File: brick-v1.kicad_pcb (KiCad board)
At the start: 2 copper layers, 28 x 41 mm, 15 parts, among them J1 buzzer_toggle_pin, J2 battery_header, U1 Teensy4.1, U2 voltReg

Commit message: v1.3 update
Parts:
- removed J2: battery_header, Connector_PinSocket_2.54mm:PinSocket_1x02_P2.54mm_Horizontal
- removed Logo0: ~, rrc_logo:RRC_logo
- removed R4: R-Device, Resistor_THT:R_Axial_DIN0207_L6.3mm_D2.5mm_P10.16mm_Horizontal
- removed S2: BN220-GPS, rrc_bn220_gps:BN220
- added Logo1: ~, rrc_logo:tmu, F.Cu at (175.8, 49.8)
- added TH1: Thermistor, Resistor_THT:R_Axial_DIN0922_L20.0mm_D9.0mm_P25.40mm_Horizontal, F.Cu at (179.1, 36.8)
- added U3: Teensy4.1, rrc_teensy:Teensy41, F.Cu at (201.9, 81.3)
- I1: value INA260 -> MPU6050; footprint rrc_INA260:INA260 -> rrc_MPU6050:MPU6050
- I2: value MPU6050 -> INA260; footprint rrc_MPU6050:MPU6050 -> rrc_INA260:INA260
- J1: value buzzer_toggle_pin -> battery_header; footprint Connector_PinHeader_2.54mm:PinHeader_1x03_P2.54mm_Vertical -> Connector_PinSocket_2.54mm:PinSocket_1x02_P2.54mm_Horizontal
- S1: value RFD900+-RF_Module -> BN220-GPS; footprint rrc_rfd900+:RFD900+ -> rrc_bn220_gps:BN220
- U1: value Teensy4.1 -> XB3-24Z8CM-J; footprint rrc_teensy:Teensy41 -> RRC_footprint:xbee_s2c
- U2: value voltReg -> L7805; footprint rrc_voltReg:voltReg2 -> Connector_PinHeader_2.54mm:PinHeader_1x03_P2.54mm_Vertical
- moved U2 107.0 mm to (221.0, 50.8)
- moved S1 71.0 mm to (175.9, 89.6)
- moved I2 70.4 mm to (201.9, 57.1)
- moved I3 56.3 mm to (166.4, 108.2)
- moved I1 53.3 mm to (158.8, 69.8)
- moved BZ1 44.6 mm to (161.3, 34.3)
- moved U1 30.9 mm to (207.9, 96.1), turned to -90 degrees
- moved J1 20.8 mm to (219.0, 34.3)
- moved R1 6.38 mm to (174.0, 60.7)
- moved R2 6.38 mm to (174.0, 64.8)
- moved R3 6.38 mm to (174.0, 68.8)
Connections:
- I1 pad 1: Net-(I1-VIN+) -> SCL2
- I1 pad 2: /V+ -> GND
- I1 pad 3: T_VCC -> SCL2
- I1 pad 4: GND -> SCL2
- I1 pad 5: SCL -> unconnected-(I1-XDA-Pad5)
- I1 pad 6: SDA -> unconnected-(I1-XCL-Pad6)
- I2 pad 1: T_VCC -> /V+
- I2 pad 2: GND -> /V-
- I2 pad 3: SCL1 -> SCL2
- I2 pad 4: SDA1 -> GND
- I2 pad 5: unconnected-(I2-XDA-Pad5) -> SCL
- I2 pad 6: unconnected-(I2-XCL-Pad6) -> SDA
- I3 pad 1: T_VCC -> SCL2
- I3 pad 4: SDA2 -> SCL2
- J1 pad 1: GND -> /V-
- J1 pad 2: Net-(J1-Pin_2) -> /V+
- R1 pad 1: SDA1 -> SCL2
- R1 pad 2: T_VCC -> SCL2
- R2 pad 1: SCL1 -> SCL2
- R2 pad 2: T_VCC -> SCL2
- R3 pad 1: SCL2 -> GND
- R3 pad 2: T_VCC -> /V-
- S1 pad 1: GND -> VCC
- S1 pad 2: GND -> TX7
- S1 pad 3: unconnected-(S1-SICTS-Pad3) -> RX7
- S1 pad 4: VCC -> GND
- U1 pad 10: unconnected-(U1-10_CS_MQSR-Pad10) -> GND
- U1 pad 2: unconnected-(U1-2_OUT2-Pad2) -> VCC
- U1 pad 22: unconnected-(U1-22_A8_CTX1-Pad22) -> (no net)
- U1 pad 30: unconnected-(U1-30_CRX3-Pad30) -> TX2
- U1 pad 31: unconnected-(U1-31_CTX3-Pad31) -> RX2
- U1 pad 33: unconnected-(U1-33_MCLK2-Pad33) -> (no net)
- U1 pad 66: unconnected-(U1-D--Pad66) -> (no net)
- U1 pad 7: RX2 -> unconnected-(U1-RSSI_PWM/DIO10-Pad7)
- U1 pad 8: TX2 -> unconnected-(U1-PWM1/DIO11-Pad8)
- U2 pad 2: /V- -> GND
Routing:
- net GND: track 0.00 -> 227.2 mm
- net SCL2: track 0.00 -> 157.9 mm
- net VCC: track 0.00 -> 144.3 mm
- net Net-(BZ1--): track 0.00 -> 120.3 mm, vias 0 -> 1
- net Net-(U3-27_A13_SCK1): track 0.00 -> 57.9 mm
- net /V-: track 0.00 -> 50.1 mm
- net RX2: track 0.00 -> 42.5 mm
- net /V+: track 0.00 -> 37.9 mm
- net TX7: track 0.00 -> 36.2 mm, vias 0 -> 1
- net RX7: track 0.00 -> 35.7 mm, vias 0 -> 1
- net TX2: track 0.00 -> 35.6 mm
- net SDA: track 0.00 -> 11.0 mm
- net SCL: track 0.00 -> 11.0 mm
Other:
- board size 28 x 41 mm -> 88.9 x 90.2 mm

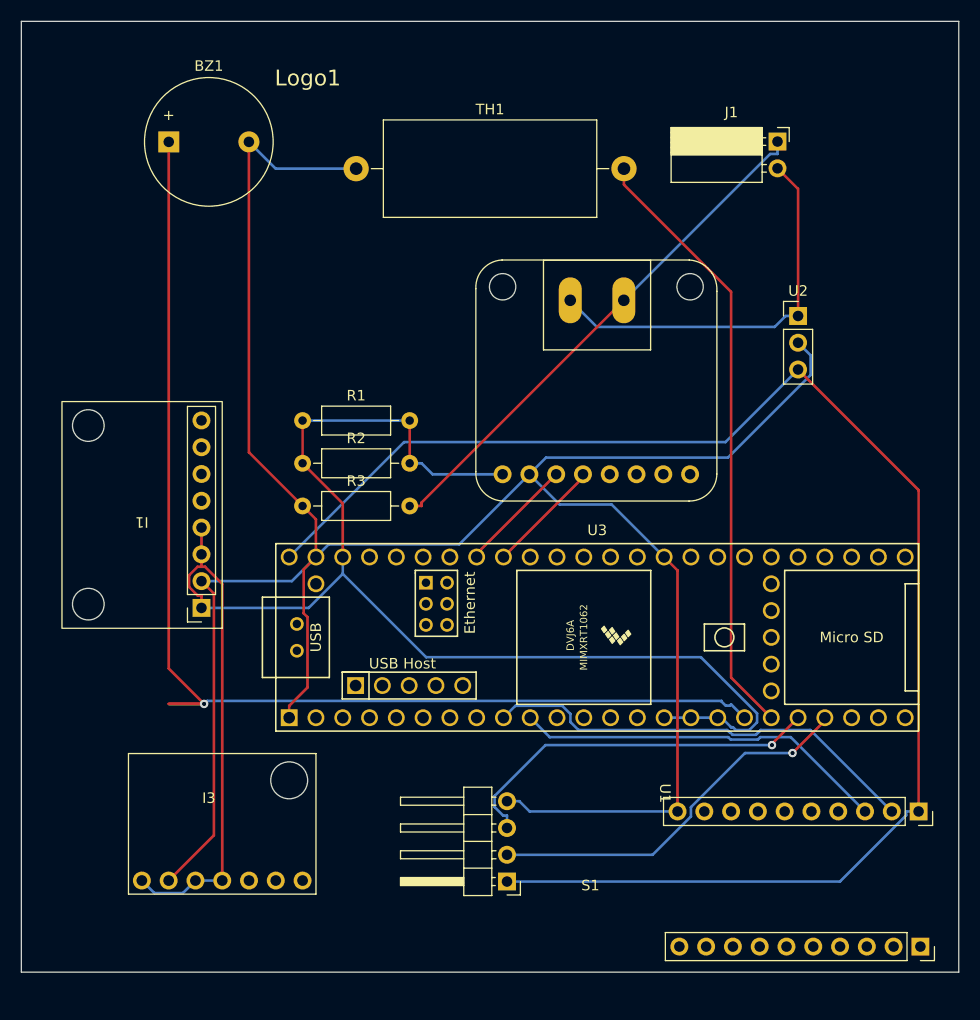
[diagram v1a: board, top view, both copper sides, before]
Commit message: updated traces
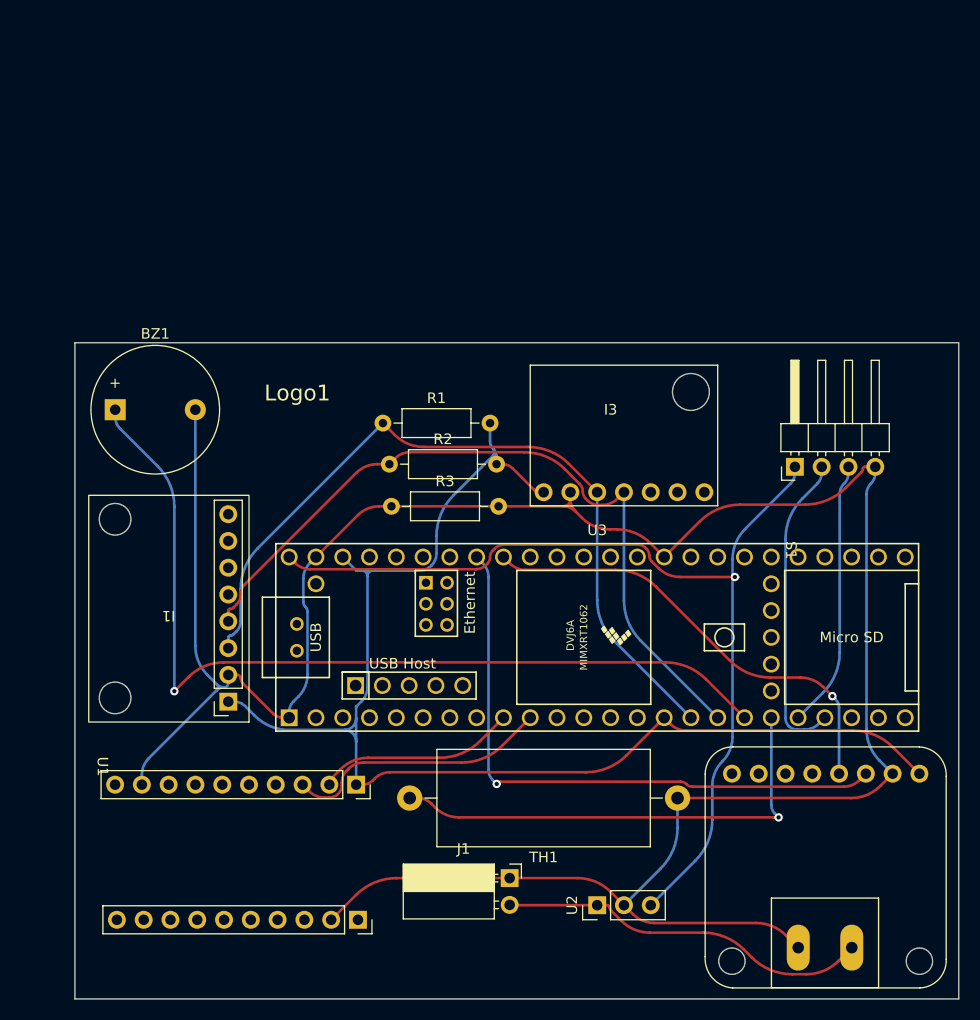
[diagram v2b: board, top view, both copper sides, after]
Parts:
- moved J1 74.3 mm to (193.6, 104.1)
- moved S1 72.9 mm to (235.6, 47.6), turned to -90 degrees
- moved TH1 67.0 mm to (209.6, 96.5), turned to 180 degrees
- moved U2 59.0 mm to (201.9, 106.7), turned to 90 degrees
- moved U1 53.4 mm to (154.5, 93.5)
- moved I3 53.0 mm to (204.5, 71.3)
- moved I2 50.6 mm to (223.5, 102.9), turned to 180 degrees
- moved BZ1 25.9 mm to (156.2, 59.7)
- moved Logo1 11.3 mm to (170.2, 59.7)
- moved I1 9.25 mm to (161.3, 78.7)
- moved R3 8.43 mm to (182.4, 68.9)
- moved R2 8.23 mm to (182.2, 64.9)
- moved R1 7.62 mm to (181.6, 61.0)
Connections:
- I1 pad 1: SCL2 -> T_VCC
- I1 pad 4: SCL2 -> SDA2
- I2 pad 2: /V- -> GND
- I2 pad 3: SCL2 -> T_VCC
- I3 pad 1: SCL2 -> T_VCC
- I3 pad 4: SCL2 -> SDA2
- J1 pad 1: /V- -> GND
- R1 pad 2: SCL2 -> T_VCC
- R2 pad 1: SCL2 -> SDA2
- R2 pad 2: SCL2 -> T_VCC
- R3 pad 2: /V- -> GND
- U1 pad 2: VCC -> T_VCC
- U1 pad 30: TX2 -> unconnected-(U1-AD1/DIO1-Pad30)
- U1 pad 31: RX2 -> unconnected-(U1-AD0/DIO0-Pad31)
- U1 pad 33: (no net) -> unconnected-(U1-RF-Pad33)
- U1 pad 4: unconnected-(U1-DIN/~{CONFIG~{/DIO14}-Pad4) -> TX2
- U3 pad 25: SCL2 -> SDA2
- U3 pad 3.3V_1: SCL2 -> T_VCC
- U3 pad 3.3V_2: SCL2 -> T_VCC
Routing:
- net T_VCC: track 0.00 -> 126.1 mm
- net SCL2: track 157.9 -> 74.6 mm
- net SDA2: track 0.00 -> 72.4 mm
- net VCC: track 144.3 -> 93.5 mm, vias 0 -> 1
- net /V-: track 50.1 -> 0.00 mm
- net SCL: track 11.0 -> 58.6 mm, vias 0 -> 1
- net Net-(BZ1--): track 120.3 -> 85.6 mm
- net SDA: track 11.0 -> 43.7 mm, vias 0 -> 1
- net RX2: track 42.5 -> 18.9 mm
- net GND: track 227.2 -> 239.5 mm
- net Net-(U3-27_A13_SCK1): track 57.9 -> 46.2 mm, vias 0 -> 1
- net RX7: track 35.7 -> 25.4 mm, vias 1 -> 0
- net TX2: track 35.6 -> 25.4 mm
- net TX7: track 36.2 -> 29.6 mm, vias 1 -> 0
- net /V+: track 37.9 -> 35.4 mm
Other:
- board size 88.9 x 90.2 mm -> 83.8 x 62.2 mm

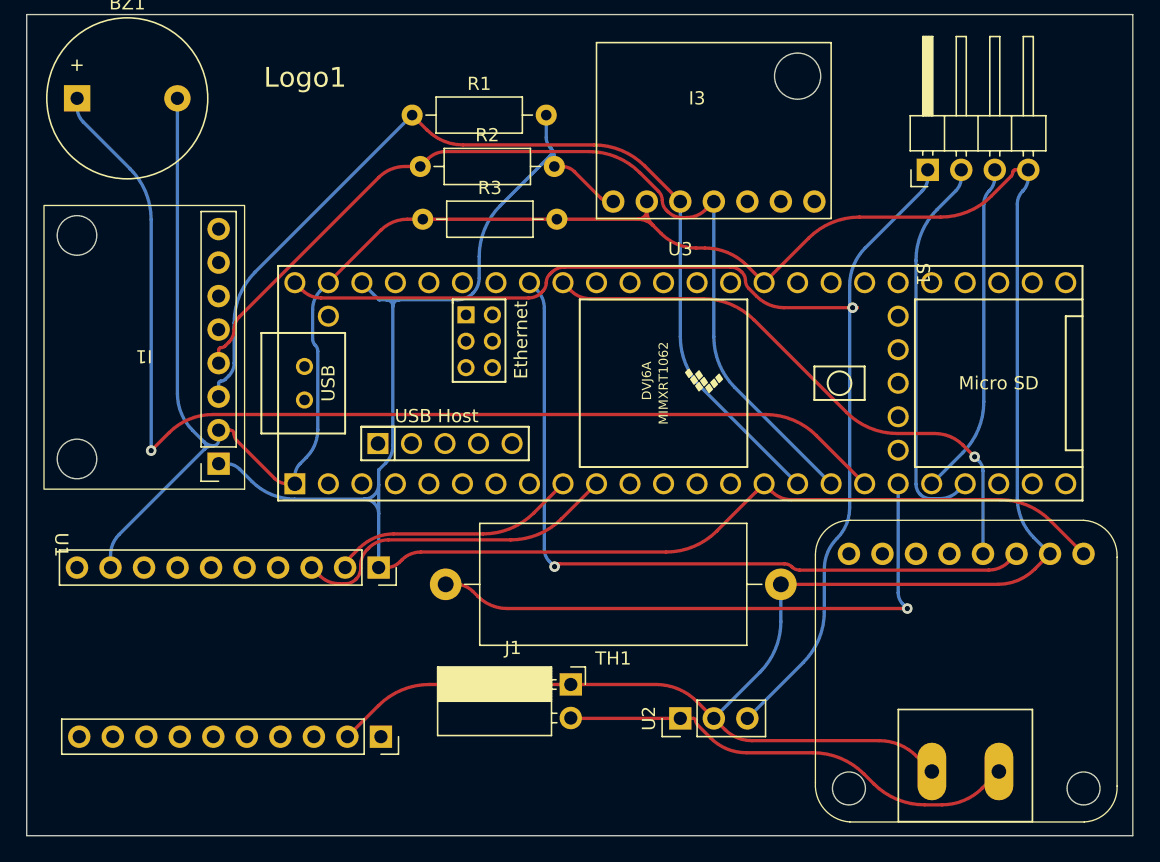
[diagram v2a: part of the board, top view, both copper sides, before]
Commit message: editted footprints and symbol of xbee
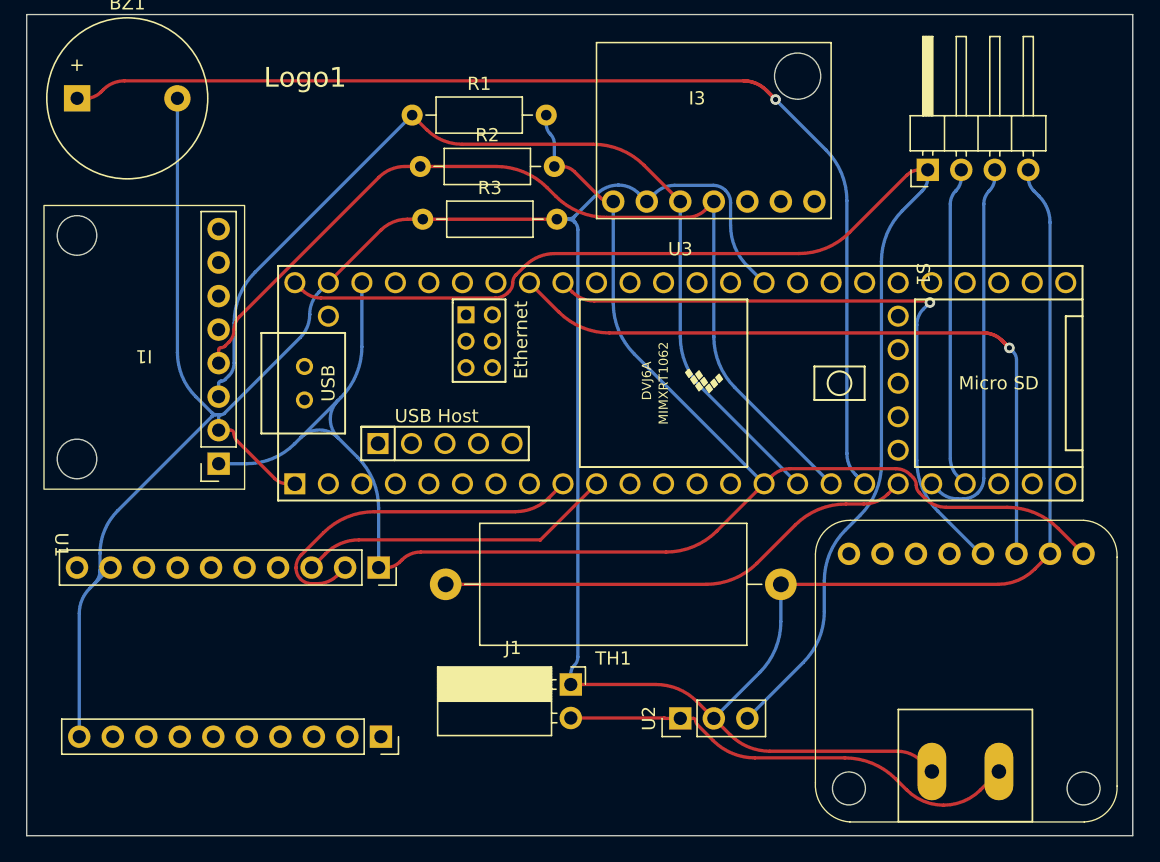
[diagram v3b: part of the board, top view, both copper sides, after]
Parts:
- U1: value XB3-24Z8CM-J -> ~
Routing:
- net Net-(U3-27_A13_SCK1): track 46.2 -> 36.8 mm, vias 1 -> 0
- net GND: track 239.5 -> 248.2 mm
- net RX2: track 18.9 -> 27.5 mm
- net SDA: track 43.7 -> 49.8 mm
- net Net-(BZ1--): track 85.6 -> 91.2 mm
- net TX7: track 29.6 -> 24.4 mm
- net T_VCC: track 126.1 -> 131.1 mm
- net VCC: track 93.5 -> 98.3 mm, vias 1 -> 0
- net RX7: track 25.4 -> 28.8 mm
- net SDA2: track 72.4 -> 71.0 mm
- net TX2: track 25.4 -> 24.0 mm

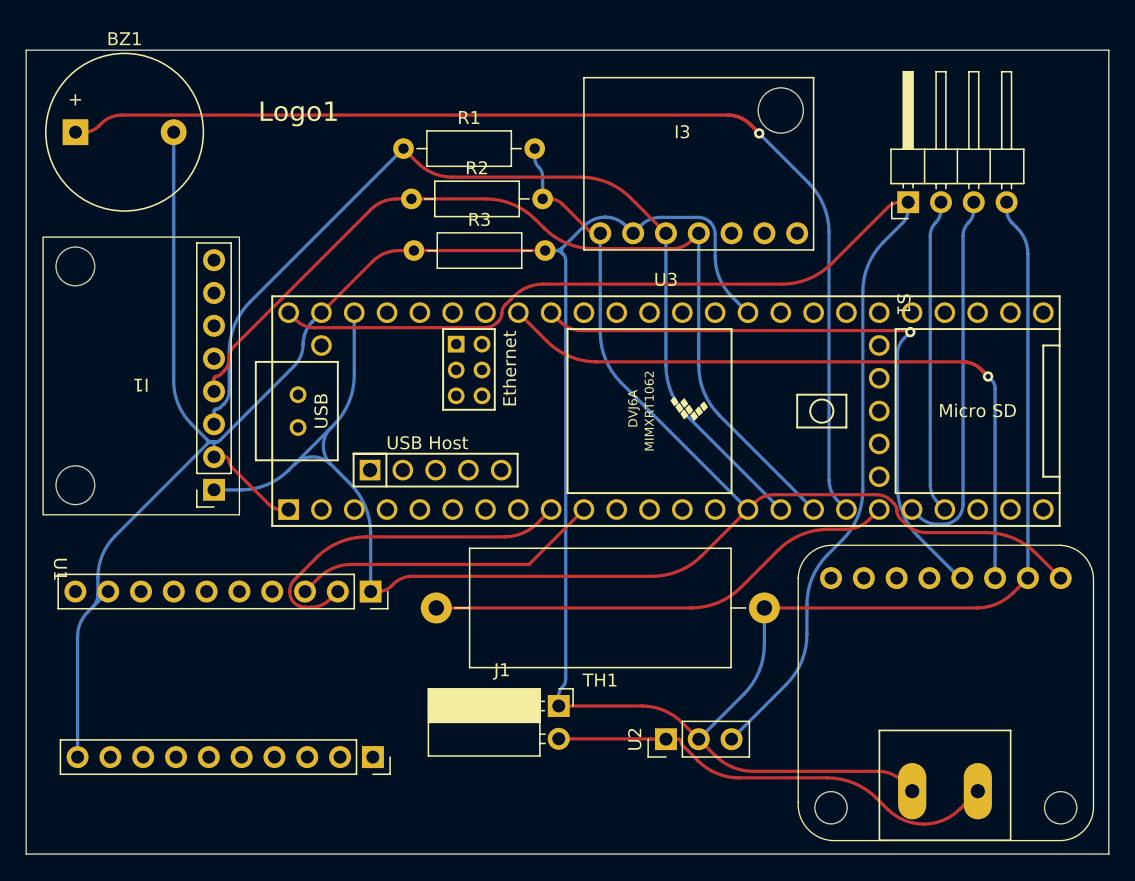
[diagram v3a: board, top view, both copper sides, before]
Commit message: reorganized and fixed component error
moved footprints around,  replaced volt reg with smaller component and deleted thermistor
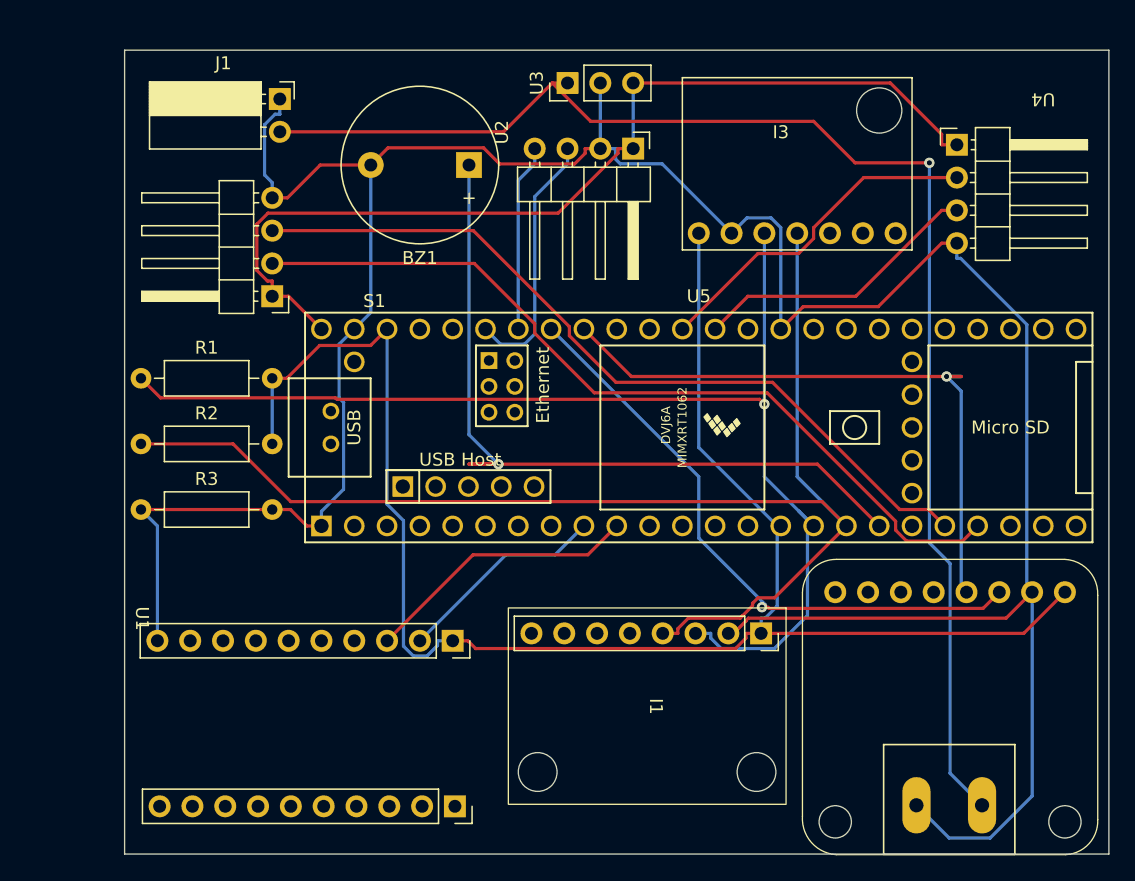
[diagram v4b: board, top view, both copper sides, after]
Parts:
- removed TH1: Thermistor, Resistor_THT:R_Axial_DIN0922_L20.0mm_D9.0mm_P25.40mm_Horizontal
- added U4: ULTRASONIC SENSOR, rrc_bn220_gps:BN220, F.Cu at (241.9, 75.5)
- added U5: Teensy4.1, rrc_teensy:Teensy41, F.Cu at (204.5, 82.5)
- U1: value ~ -> XBEE S2C PRO
- U2: value L7805 -> esp32; footprint Connector_PinHeader_2.54mm:PinHeader_1x03_P2.54mm_Vertical -> rrc_bn220_gps:BN220
- U3: value Teensy4.1 -> L7805; footprint rrc_teensy:Teensy41 -> Connector_PinHeader_2.54mm:PinHeader_1x03_P2.54mm_Vertical
- moved S1 82.2 mm to (154.0, 57.5), turned to 0 degrees
- moved J1 51.7 mm to (172.0, 57.1)
- moved I1 46.9 mm to (200.7, 104.1), turned to -90 degrees
- moved Logo1 38.4 mm to (201.9, 81.3)
- moved U2 33.2 mm to (184.5, 78.5)
- moved BZ1 30.6 mm to (186.7, 62.2), turned to 180 degrees
- moved R3 29.1 mm to (161.3, 88.9)
- moved R2 28.2 mm to (161.3, 83.8)
- moved R1 27.0 mm to (161.3, 78.7)
- moved U3 26.5 mm to (194.3, 55.9), turned to 90 degrees
- moved I3 7.62 mm to (212.1, 71.3)
- moved U1 7.41 mm to (160.9, 97.3)
- moved I2 1.14 mm to (223.8, 104.0)
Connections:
- U1 pad 17: (no net) -> unconnected-(U1-VREF-Pad17)
- U1 pad 18: (no net) -> unconnected-(U1-ON-Pad18)
- U1 pad 19: (no net) -> unconnected-(U1-CTS-Pad19)
- U1 pad 2: T_VCC -> RX2
- U1 pad 20: (no net) -> unconnected-(U1-AD4-Pad20)
- U1 pad 3: RX2 -> TX2
- U1 pad 4: TX2 -> unconnected-(U1-DO8-Pad4)
- U2 pad 1: /V+ -> VCC
- U2 pad 3: VCC -> RX5
- U3 pad 1: unconnected-(U3-1_TX1_CTX2_MISO1-Pad1) -> /V+
- U3 pad 2: unconnected-(U3-2_OUT2-Pad2) -> GND
- U3 pad 3: unconnected-(U3-3_LRCLK2-Pad3) -> VCC
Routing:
- net /V+: track 35.5 -> 107.0 mm, vias 0 -> 1
- net TX7: track 24.4 -> 64.8 mm
- net Net-(U3-27_A13_SCK1): track 36.8 -> 0.00 mm
- net RX7: track 28.8 -> 62.0 mm
- net SDA2: track 71.0 -> 99.7 mm
- net GND: track 248.2 -> 220.7 mm
- net A1: track 0.00 -> 26.6 mm
- net Net-(BZ1--): track 91.2 -> 64.7 mm
- net VCC: track 98.3 -> 75.5 mm
- net A0: track 0.00 -> 22.5 mm
- net RX5: track 0.00 -> 20.0 mm
- net SCL2: track 74.6 -> 92.1 mm, vias 0 -> 1
- net TX5: track 0.00 -> 14.5 mm
- net RX2: track 27.5 -> 16.4 mm
- net SCL: track 58.6 -> 47.6 mm
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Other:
- board size 83.8 x 62.2 mm -> 76.2 x 62.2 mm
